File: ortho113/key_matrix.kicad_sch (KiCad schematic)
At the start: 226 parts

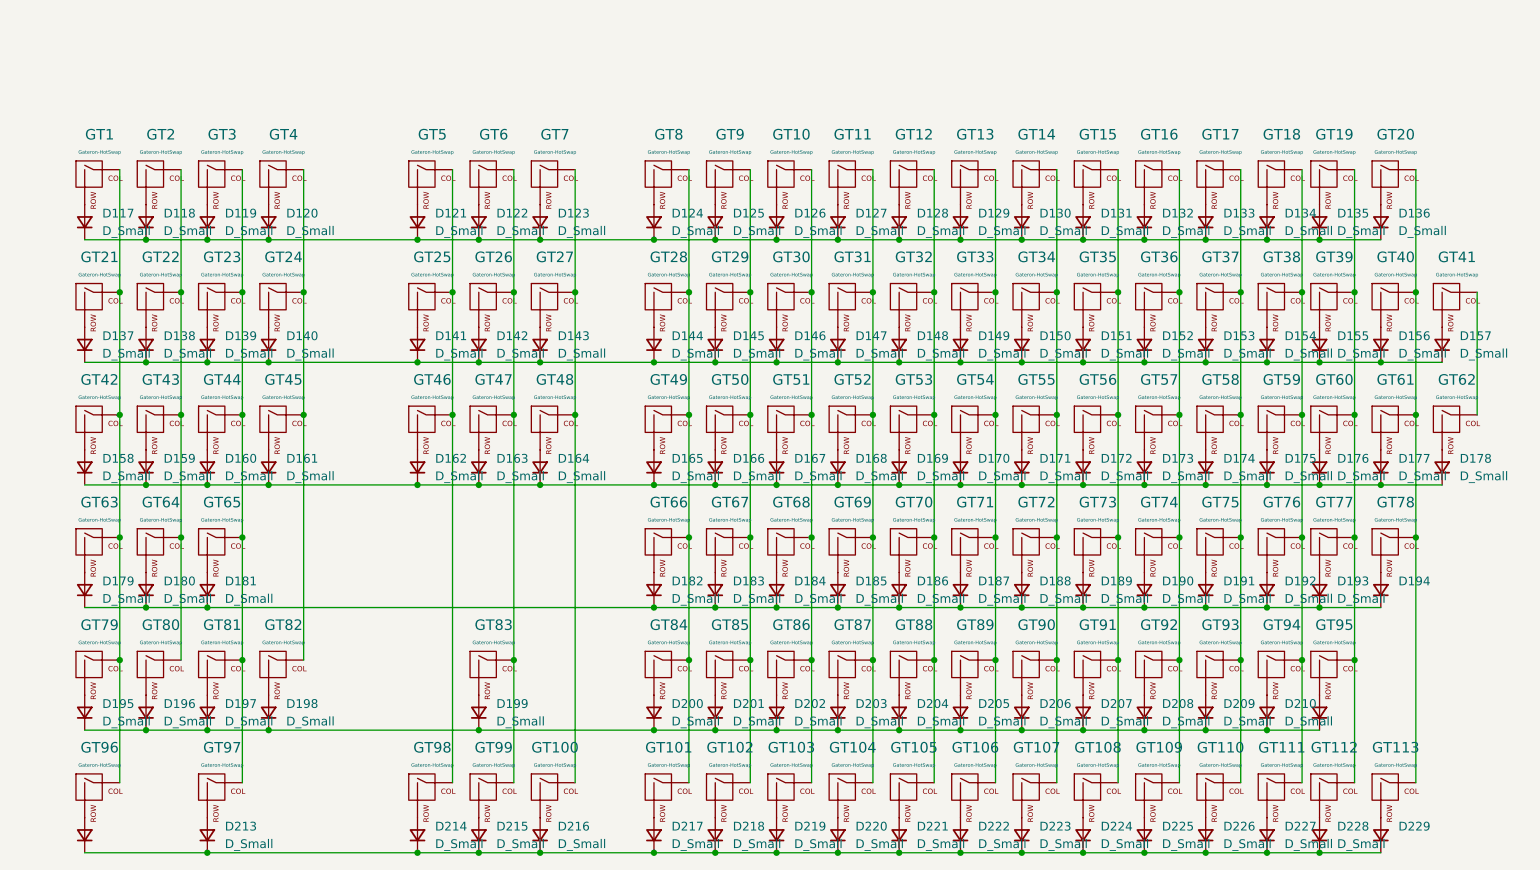
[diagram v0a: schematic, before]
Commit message: fixed submodule conflict & remove gitignore
added pinout for oled display
finished rev1 of pcb design
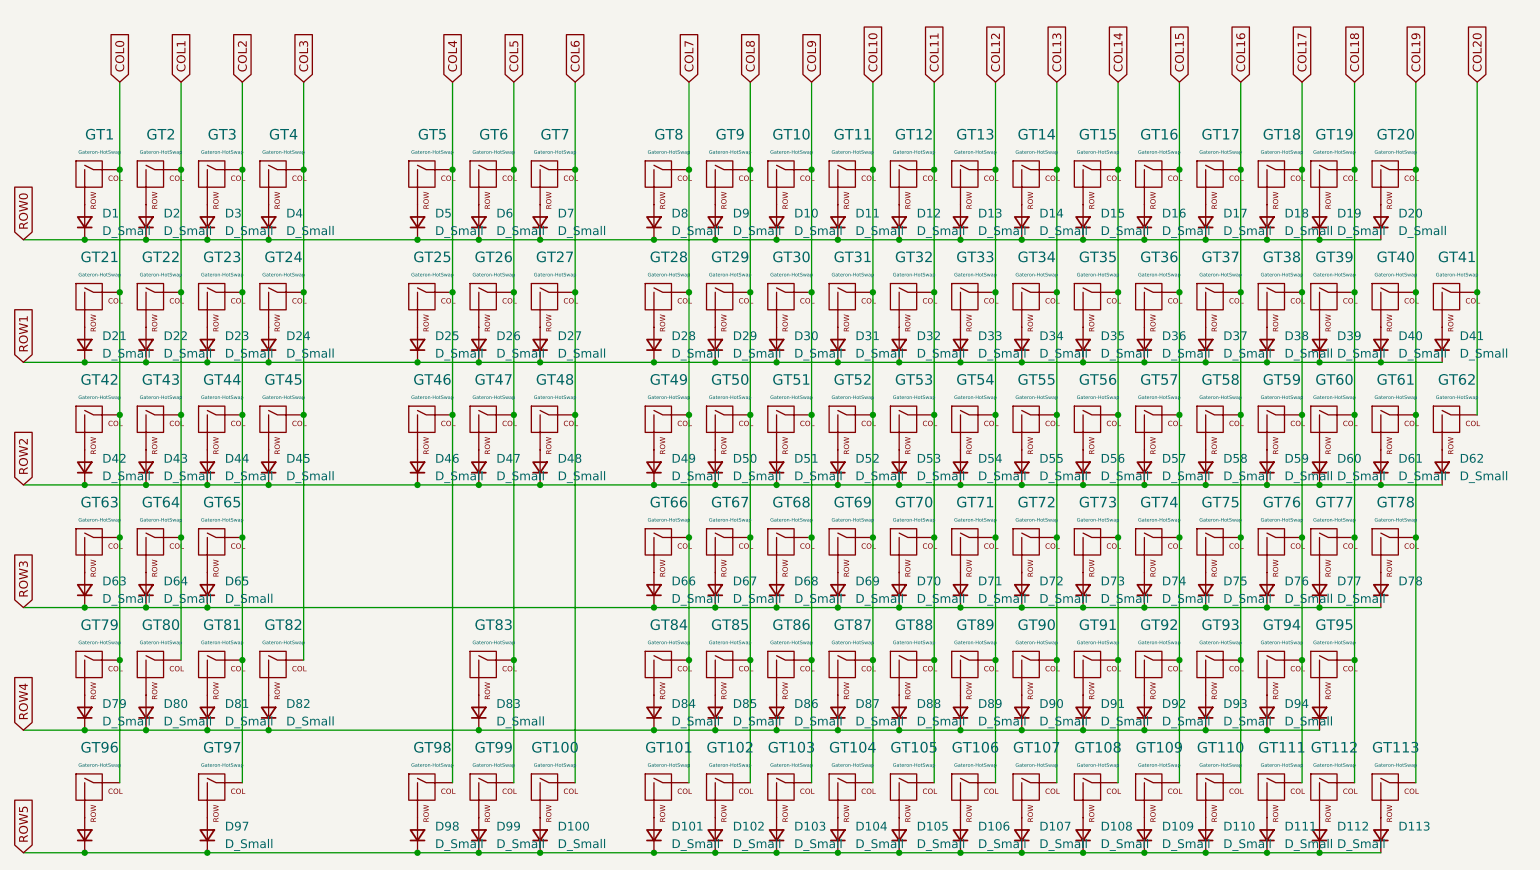
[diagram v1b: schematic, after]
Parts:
- D1: renamed from D117; footprint random-keyboard-parts:D_SOD-123-Pretty -> my-footprints:D_SOD-123-Pretty-symbol
- D10: renamed from D126; footprint random-keyboard-parts:D_SOD-123-Pretty -> my-footprints:D_SOD-123-Pretty-symbol
- D100: renamed from D216; footprint random-keyboard-parts:D_SOD-123-Pretty -> my-footprints:D_SOD-123-Pretty-symbol
- D101: renamed from D217; footprint random-keyboard-parts:D_SOD-123-Pretty -> my-footprints:D_SOD-123-Pretty-symbol
- D102: renamed from D218; footprint random-keyboard-parts:D_SOD-123-Pretty -> my-footprints:D_SOD-123-Pretty-symbol
- D103: renamed from D219; footprint random-keyboard-parts:D_SOD-123-Pretty -> my-footprints:D_SOD-123-Pretty-symbol
- D104: renamed from D220; footprint random-keyboard-parts:D_SOD-123-Pretty -> my-footprints:D_SOD-123-Pretty-symbol
- D105: renamed from D221; footprint random-keyboard-parts:D_SOD-123-Pretty -> my-footprints:D_SOD-123-Pretty-symbol
- D106: renamed from D222; footprint random-keyboard-parts:D_SOD-123-Pretty -> my-footprints:D_SOD-123-Pretty-symbol
- D107: renamed from D223; footprint random-keyboard-parts:D_SOD-123-Pretty -> my-footprints:D_SOD-123-Pretty-symbol
- D108: renamed from D224; footprint random-keyboard-parts:D_SOD-123-Pretty -> my-footprints:D_SOD-123-Pretty-symbol
- D109: renamed from D225; footprint random-keyboard-parts:D_SOD-123-Pretty -> my-footprints:D_SOD-123-Pretty-symbol
- D11: renamed from D127; footprint random-keyboard-parts:D_SOD-123-Pretty -> my-footprints:D_SOD-123-Pretty-symbol
- D110: renamed from D226; footprint random-keyboard-parts:D_SOD-123-Pretty -> my-footprints:D_SOD-123-Pretty-symbol
- D111: renamed from D227; footprint random-keyboard-parts:D_SOD-123-Pretty -> my-footprints:D_SOD-123-Pretty-symbol
- D112: renamed from D228; footprint random-keyboard-parts:D_SOD-123-Pretty -> my-footprints:D_SOD-123-Pretty-symbol
- D113: renamed from D229; footprint random-keyboard-parts:D_SOD-123-Pretty -> my-footprints:D_SOD-123-Pretty-symbol
- D12: renamed from D128; footprint random-keyboard-parts:D_SOD-123-Pretty -> my-footprints:D_SOD-123-Pretty-symbol
- D13: renamed from D129; footprint random-keyboard-parts:D_SOD-123-Pretty -> my-footprints:D_SOD-123-Pretty-symbol
- D14: renamed from D130; footprint random-keyboard-parts:D_SOD-123-Pretty -> my-footprints:D_SOD-123-Pretty-symbol
- D15: renamed from D131; footprint random-keyboard-parts:D_SOD-123-Pretty -> my-footprints:D_SOD-123-Pretty-symbol
- D16: renamed from D132; footprint random-keyboard-parts:D_SOD-123-Pretty -> my-footprints:D_SOD-123-Pretty-symbol
- D17: renamed from D133; footprint random-keyboard-parts:D_SOD-123-Pretty -> my-footprints:D_SOD-123-Pretty-symbol
- D18: renamed from D134; footprint random-keyboard-parts:D_SOD-123-Pretty -> my-footprints:D_SOD-123-Pretty-symbol
- D19: renamed from D135; footprint random-keyboard-parts:D_SOD-123-Pretty -> my-footprints:D_SOD-123-Pretty-symbol
- D2: renamed from D118; footprint random-keyboard-parts:D_SOD-123-Pretty -> my-footprints:D_SOD-123-Pretty-symbol
- D20: renamed from D136; footprint random-keyboard-parts:D_SOD-123-Pretty -> my-footprints:D_SOD-123-Pretty-symbol
- D21: renamed from D137; footprint random-keyboard-parts:D_SOD-123-Pretty -> my-footprints:D_SOD-123-Pretty-symbol
- D22: renamed from D138; footprint random-keyboard-parts:D_SOD-123-Pretty -> my-footprints:D_SOD-123-Pretty-symbol
- D23: renamed from D139; footprint random-keyboard-parts:D_SOD-123-Pretty -> my-footprints:D_SOD-123-Pretty-symbol
- D24: renamed from D140; footprint random-keyboard-parts:D_SOD-123-Pretty -> my-footprints:D_SOD-123-Pretty-symbol
- D25: renamed from D141; footprint random-keyboard-parts:D_SOD-123-Pretty -> my-footprints:D_SOD-123-Pretty-symbol
- D26: renamed from D142; footprint random-keyboard-parts:D_SOD-123-Pretty -> my-footprints:D_SOD-123-Pretty-symbol
- D27: renamed from D143; footprint random-keyboard-parts:D_SOD-123-Pretty -> my-footprints:D_SOD-123-Pretty-symbol
- D28: renamed from D144; footprint random-keyboard-parts:D_SOD-123-Pretty -> my-footprints:D_SOD-123-Pretty-symbol
- D29: renamed from D145; footprint random-keyboard-parts:D_SOD-123-Pretty -> my-footprints:D_SOD-123-Pretty-symbol
- D3: renamed from D119; footprint random-keyboard-parts:D_SOD-123-Pretty -> my-footprints:D_SOD-123-Pretty-symbol
- D30: renamed from D146; footprint random-keyboard-parts:D_SOD-123-Pretty -> my-footprints:D_SOD-123-Pretty-symbol
- D31: renamed from D147; footprint random-keyboard-parts:D_SOD-123-Pretty -> my-footprints:D_SOD-123-Pretty-symbol
- D32: renamed from D148; footprint random-keyboard-parts:D_SOD-123-Pretty -> my-footprints:D_SOD-123-Pretty-symbol
- D33: renamed from D149; footprint random-keyboard-parts:D_SOD-123-Pretty -> my-footprints:D_SOD-123-Pretty-symbol
- D34: renamed from D150; footprint random-keyboard-parts:D_SOD-123-Pretty -> my-footprints:D_SOD-123-Pretty-symbol
- D35: renamed from D151; footprint random-keyboard-parts:D_SOD-123-Pretty -> my-footprints:D_SOD-123-Pretty-symbol
- D36: renamed from D152; footprint random-keyboard-parts:D_SOD-123-Pretty -> my-footprints:D_SOD-123-Pretty-symbol
- D37: renamed from D153; footprint random-keyboard-parts:D_SOD-123-Pretty -> my-footprints:D_SOD-123-Pretty-symbol
- D38: renamed from D154; footprint random-keyboard-parts:D_SOD-123-Pretty -> my-footprints:D_SOD-123-Pretty-symbol
- D39: renamed from D155; footprint random-keyboard-parts:D_SOD-123-Pretty -> my-footprints:D_SOD-123-Pretty-symbol
- D4: renamed from D120; footprint random-keyboard-parts:D_SOD-123-Pretty -> my-footprints:D_SOD-123-Pretty-symbol
- D40: renamed from D156; footprint random-keyboard-parts:D_SOD-123-Pretty -> my-footprints:D_SOD-123-Pretty-symbol
- D41: renamed from D157; footprint random-keyboard-parts:D_SOD-123-Pretty -> my-footprints:D_SOD-123-Pretty-symbol
- D42: renamed from D158; footprint random-keyboard-parts:D_SOD-123-Pretty -> my-footprints:D_SOD-123-Pretty-symbol
- D43: renamed from D159; footprint random-keyboard-parts:D_SOD-123-Pretty -> my-footprints:D_SOD-123-Pretty-symbol
- D44: renamed from D160; footprint random-keyboard-parts:D_SOD-123-Pretty -> my-footprints:D_SOD-123-Pretty-symbol
- D45: renamed from D161; footprint random-keyboard-parts:D_SOD-123-Pretty -> my-footprints:D_SOD-123-Pretty-symbol
- D46: renamed from D162; footprint random-keyboard-parts:D_SOD-123-Pretty -> my-footprints:D_SOD-123-Pretty-symbol
- D47: renamed from D163; footprint random-keyboard-parts:D_SOD-123-Pretty -> my-footprints:D_SOD-123-Pretty-symbol
- D48: renamed from D164; footprint random-keyboard-parts:D_SOD-123-Pretty -> my-footprints:D_SOD-123-Pretty-symbol
- D49: renamed from D165; footprint random-keyboard-parts:D_SOD-123-Pretty -> my-footprints:D_SOD-123-Pretty-symbol
- D5: renamed from D121; footprint random-keyboard-parts:D_SOD-123-Pretty -> my-footprints:D_SOD-123-Pretty-symbol
- D50: renamed from D166; footprint random-keyboard-parts:D_SOD-123-Pretty -> my-footprints:D_SOD-123-Pretty-symbol
- D51: renamed from D167; footprint random-keyboard-parts:D_SOD-123-Pretty -> my-footprints:D_SOD-123-Pretty-symbol
- D52: renamed from D168; footprint random-keyboard-parts:D_SOD-123-Pretty -> my-footprints:D_SOD-123-Pretty-symbol
- D53: renamed from D169; footprint random-keyboard-parts:D_SOD-123-Pretty -> my-footprints:D_SOD-123-Pretty-symbol
- D54: renamed from D170; footprint random-keyboard-parts:D_SOD-123-Pretty -> my-footprints:D_SOD-123-Pretty-symbol
- D55: renamed from D171; footprint random-keyboard-parts:D_SOD-123-Pretty -> my-footprints:D_SOD-123-Pretty-symbol
- D56: renamed from D172; footprint random-keyboard-parts:D_SOD-123-Pretty -> my-footprints:D_SOD-123-Pretty-symbol
- D57: renamed from D173; footprint random-keyboard-parts:D_SOD-123-Pretty -> my-footprints:D_SOD-123-Pretty-symbol
- D58: renamed from D174; footprint random-keyboard-parts:D_SOD-123-Pretty -> my-footprints:D_SOD-123-Pretty-symbol
- D59: renamed from D175; footprint random-keyboard-parts:D_SOD-123-Pretty -> my-footprints:D_SOD-123-Pretty-symbol
- D6: renamed from D122; footprint random-keyboard-parts:D_SOD-123-Pretty -> my-footprints:D_SOD-123-Pretty-symbol
- D60: renamed from D176; footprint random-keyboard-parts:D_SOD-123-Pretty -> my-footprints:D_SOD-123-Pretty-symbol
- D61: renamed from D177; footprint random-keyboard-parts:D_SOD-123-Pretty -> my-footprints:D_SOD-123-Pretty-symbol
- D62: renamed from D178; footprint random-keyboard-parts:D_SOD-123-Pretty -> my-footprints:D_SOD-123-Pretty-symbol
- D63: renamed from D179; footprint random-keyboard-parts:D_SOD-123-Pretty -> my-footprints:D_SOD-123-Pretty-symbol
- D64: renamed from D180; footprint random-keyboard-parts:D_SOD-123-Pretty -> my-footprints:D_SOD-123-Pretty-symbol
- D65: renamed from D181; footprint random-keyboard-parts:D_SOD-123-Pretty -> my-footprints:D_SOD-123-Pretty-symbol
- D66: renamed from D182; footprint random-keyboard-parts:D_SOD-123-Pretty -> my-footprints:D_SOD-123-Pretty-symbol
- D67: renamed from D183; footprint random-keyboard-parts:D_SOD-123-Pretty -> my-footprints:D_SOD-123-Pretty-symbol
- D68: renamed from D184; footprint random-keyboard-parts:D_SOD-123-Pretty -> my-footprints:D_SOD-123-Pretty-symbol
- D69: renamed from D185; footprint random-keyboard-parts:D_SOD-123-Pretty -> my-footprints:D_SOD-123-Pretty-symbol
- D7: renamed from D123; footprint random-keyboard-parts:D_SOD-123-Pretty -> my-footprints:D_SOD-123-Pretty-symbol
- D70: renamed from D186; footprint random-keyboard-parts:D_SOD-123-Pretty -> my-footprints:D_SOD-123-Pretty-symbol
- D71: renamed from D187; footprint random-keyboard-parts:D_SOD-123-Pretty -> my-footprints:D_SOD-123-Pretty-symbol
- D72: renamed from D188; footprint random-keyboard-parts:D_SOD-123-Pretty -> my-footprints:D_SOD-123-Pretty-symbol
- D73: renamed from D189; footprint random-keyboard-parts:D_SOD-123-Pretty -> my-footprints:D_SOD-123-Pretty-symbol
- D74: renamed from D190; footprint random-keyboard-parts:D_SOD-123-Pretty -> my-footprints:D_SOD-123-Pretty-symbol
- D75: renamed from D191; footprint random-keyboard-parts:D_SOD-123-Pretty -> my-footprints:D_SOD-123-Pretty-symbol
- D76: renamed from D192; footprint random-keyboard-parts:D_SOD-123-Pretty -> my-footprints:D_SOD-123-Pretty-symbol
- D77: renamed from D193; footprint random-keyboard-parts:D_SOD-123-Pretty -> my-footprints:D_SOD-123-Pretty-symbol
- D78: renamed from D194; footprint random-keyboard-parts:D_SOD-123-Pretty -> my-footprints:D_SOD-123-Pretty-symbol
- D79: renamed from D195; footprint random-keyboard-parts:D_SOD-123-Pretty -> my-footprints:D_SOD-123-Pretty-symbol
- D8: renamed from D124; footprint random-keyboard-parts:D_SOD-123-Pretty -> my-footprints:D_SOD-123-Pretty-symbol
- D80: renamed from D196; footprint random-keyboard-parts:D_SOD-123-Pretty -> my-footprints:D_SOD-123-Pretty-symbol
- D81: renamed from D197; footprint random-keyboard-parts:D_SOD-123-Pretty -> my-footprints:D_SOD-123-Pretty-symbol
- D82: renamed from D198; footprint random-keyboard-parts:D_SOD-123-Pretty -> my-footprints:D_SOD-123-Pretty-symbol
- D83: renamed from D199; footprint random-keyboard-parts:D_SOD-123-Pretty -> my-footprints:D_SOD-123-Pretty-symbol
- D84: renamed from D200; footprint random-keyboard-parts:D_SOD-123-Pretty -> my-footprints:D_SOD-123-Pretty-symbol
- D85: renamed from D201; footprint random-keyboard-parts:D_SOD-123-Pretty -> my-footprints:D_SOD-123-Pretty-symbol
- D86: renamed from D202; footprint random-keyboard-parts:D_SOD-123-Pretty -> my-footprints:D_SOD-123-Pretty-symbol
- D87: renamed from D203; footprint random-keyboard-parts:D_SOD-123-Pretty -> my-footprints:D_SOD-123-Pretty-symbol
- D88: renamed from D204; footprint random-keyboard-parts:D_SOD-123-Pretty -> my-footprints:D_SOD-123-Pretty-symbol
- D89: renamed from D205; footprint random-keyboard-parts:D_SOD-123-Pretty -> my-footprints:D_SOD-123-Pretty-symbol
- D9: renamed from D125; footprint random-keyboard-parts:D_SOD-123-Pretty -> my-footprints:D_SOD-123-Pretty-symbol
- D90: renamed from D206; footprint random-keyboard-parts:D_SOD-123-Pretty -> my-footprints:D_SOD-123-Pretty-symbol
- D91: renamed from D207; footprint random-keyboard-parts:D_SOD-123-Pretty -> my-footprints:D_SOD-123-Pretty-symbol
- D92: renamed from D208; footprint random-keyboard-parts:D_SOD-123-Pretty -> my-footprints:D_SOD-123-Pretty-symbol
- D93: renamed from D209; footprint random-keyboard-parts:D_SOD-123-Pretty -> my-footprints:D_SOD-123-Pretty-symbol
- D94: renamed from D210; footprint random-keyboard-parts:D_SOD-123-Pretty -> my-footprints:D_SOD-123-Pretty-symbol
- D95: renamed from D211; footprint random-keyboard-parts:D_SOD-123-Pretty -> my-footprints:D_SOD-123-Pretty-symbol
- D96: renamed from D212; footprint random-keyboard-parts:D_SOD-123-Pretty -> my-footprints:D_SOD-123-Pretty-symbol
- D97: renamed from D213; footprint random-keyboard-parts:D_SOD-123-Pretty -> my-footprints:D_SOD-123-Pretty-symbol
- D98: renamed from D214; footprint random-keyboard-parts:D_SOD-123-Pretty -> my-footprints:D_SOD-123-Pretty-symbol
- D99: renamed from D215; footprint random-keyboard-parts:D_SOD-123-Pretty -> my-footprints:D_SOD-123-Pretty-symbol
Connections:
- net ROW2: now reaches D42.1 (K), D43.1 (K), D44.1 (K), D45.1 (K), D46.1 (K), D47.1 (K), D48.1 (K), D49.1 (K), D50.1 (K), D51.1 (K), D52.1 (K), D53.1 (K), D54.1 (K), D55.1 (K), D56.1 (K), D57.1 (K), D58.1 (K), D59.1 (K), D60.1 (K), D61.1 (K), D62.1 (K)
- net COL18: now reaches GT112.1 (COL), GT19.1 (COL), GT39.1 (COL), GT60.1 (COL), GT77.1 (COL), GT95.1 (COL)
- net COL7: now reaches GT101.1 (COL), GT28.1 (COL), GT49.1 (COL), GT66.1 (COL), GT8.1 (COL), GT84.1 (COL)
- net COL14: now reaches GT108.1 (COL), GT15.1 (COL), GT35.1 (COL), GT56.1 (COL), GT73.1 (COL), GT91.1 (COL)
- net COL11: now reaches GT105.1 (COL), GT12.1 (COL), GT32.1 (COL), GT53.1 (COL), GT70.1 (COL), GT88.1 (COL)
- net ROW0: now reaches D1.1 (K), D10.1 (K), D11.1 (K), D12.1 (K), D13.1 (K), D14.1 (K), D15.1 (K), D16.1 (K), D17.1 (K), D18.1 (K), D19.1 (K), D2.1 (K), D20.1 (K), D3.1 (K), D4.1 (K), D5.1 (K), D6.1 (K), D7.1 (K), D8.1 (K), D9.1 (K)
- net COL20: now reaches GT41.1 (COL), GT62.1 (COL)
- net COL19: now reaches GT113.1 (COL), GT20.1 (COL), GT40.1 (COL), GT61.1 (COL), GT78.1 (COL)
- net COL12: now reaches GT106.1 (COL), GT13.1 (COL), GT33.1 (COL), GT54.1 (COL), GT71.1 (COL), GT89.1 (COL)
- net ROW1: now reaches D21.1 (K), D22.1 (K), D23.1 (K), D24.1 (K), D25.1 (K), D26.1 (K), D27.1 (K), D28.1 (K), D29.1 (K), D30.1 (K), D31.1 (K), D32.1 (K), D33.1 (K), D34.1 (K), D35.1 (K), D36.1 (K), D37.1 (K), D38.1 (K), D39.1 (K), D40.1 (K), D41.1 (K)
- net ROW5: now reaches D100.1 (K), D101.1 (K), D102.1 (K), D103.1 (K), D104.1 (K), D105.1 (K), D106.1 (K), D107.1 (K), D108.1 (K), D109.1 (K), D110.1 (K), D111.1 (K), D112.1 (K), D113.1 (K), D96.1 (K), D97.1 (K), D98.1 (K), D99.1 (K)
- net COL9: now reaches GT10.1 (COL), GT103.1 (COL), GT30.1 (COL), GT51.1 (COL), GT68.1 (COL), GT86.1 (COL)
- net ROW4: now reaches D79.1 (K), D80.1 (K), D81.1 (K), D82.1 (K), D83.1 (K), D84.1 (K), D85.1 (K), D86.1 (K), D87.1 (K), D88.1 (K), D89.1 (K), D90.1 (K), D91.1 (K), D92.1 (K), D93.1 (K), D94.1 (K), D95.1 (K)
- net ROW3: now reaches D63.1 (K), D64.1 (K), D65.1 (K), D66.1 (K), D67.1 (K), D68.1 (K), D69.1 (K), D70.1 (K), D71.1 (K), D72.1 (K), D73.1 (K), D74.1 (K), D75.1 (K), D76.1 (K), D77.1 (K), D78.1 (K)
- net COL15: now reaches GT109.1 (COL), GT16.1 (COL), GT36.1 (COL), GT57.1 (COL), GT74.1 (COL), GT92.1 (COL)
- net COL8: now reaches GT102.1 (COL), GT29.1 (COL), GT50.1 (COL), GT67.1 (COL), GT85.1 (COL), GT9.1 (COL)
- net COL16: now reaches GT110.1 (COL), GT17.1 (COL), GT37.1 (COL), GT58.1 (COL), GT75.1 (COL), GT93.1 (COL)
- net COL3: now reaches GT24.1 (COL), GT4.1 (COL), GT45.1 (COL), GT82.1 (COL)
- net COL0: now reaches GT1.1 (COL), GT21.1 (COL), GT42.1 (COL), GT63.1 (COL), GT79.1 (COL), GT96.1 (COL)
- net COL17: now reaches GT111.1 (COL), GT18.1 (COL), GT38.1 (COL), GT59.1 (COL), GT76.1 (COL), GT94.1 (COL)
- net COL10: now reaches GT104.1 (COL), GT11.1 (COL), GT31.1 (COL), GT52.1 (COL), GT69.1 (COL), GT87.1 (COL)
- net COL2: now reaches GT23.1 (COL), GT3.1 (COL), GT44.1 (COL), GT65.1 (COL), GT81.1 (COL), GT97.1 (COL)
- net COL13: now reaches GT107.1 (COL), GT14.1 (COL), GT34.1 (COL), GT55.1 (COL), GT72.1 (COL), GT90.1 (COL)
- net COL1: now reaches GT2.1 (COL), GT22.1 (COL), GT43.1 (COL), GT64.1 (COL), GT80.1 (COL)
- net COL4: now reaches GT25.1 (COL), GT46.1 (COL), GT5.1 (COL), GT98.1 (COL)
- net COL5: now reaches GT26.1 (COL), GT47.1 (COL), GT6.1 (COL), GT83.1 (COL), GT99.1 (COL)
- net COL6: now reaches GT100.1 (COL), GT27.1 (COL), GT48.1 (COL), GT7.1 (COL)
